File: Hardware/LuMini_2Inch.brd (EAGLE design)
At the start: 54.2 x 54.2 mm, 73 parts, among them J1 SOLDER_PAD_2, J2 SOLDER_PAD_2, J3 SOLDER_PAD_2

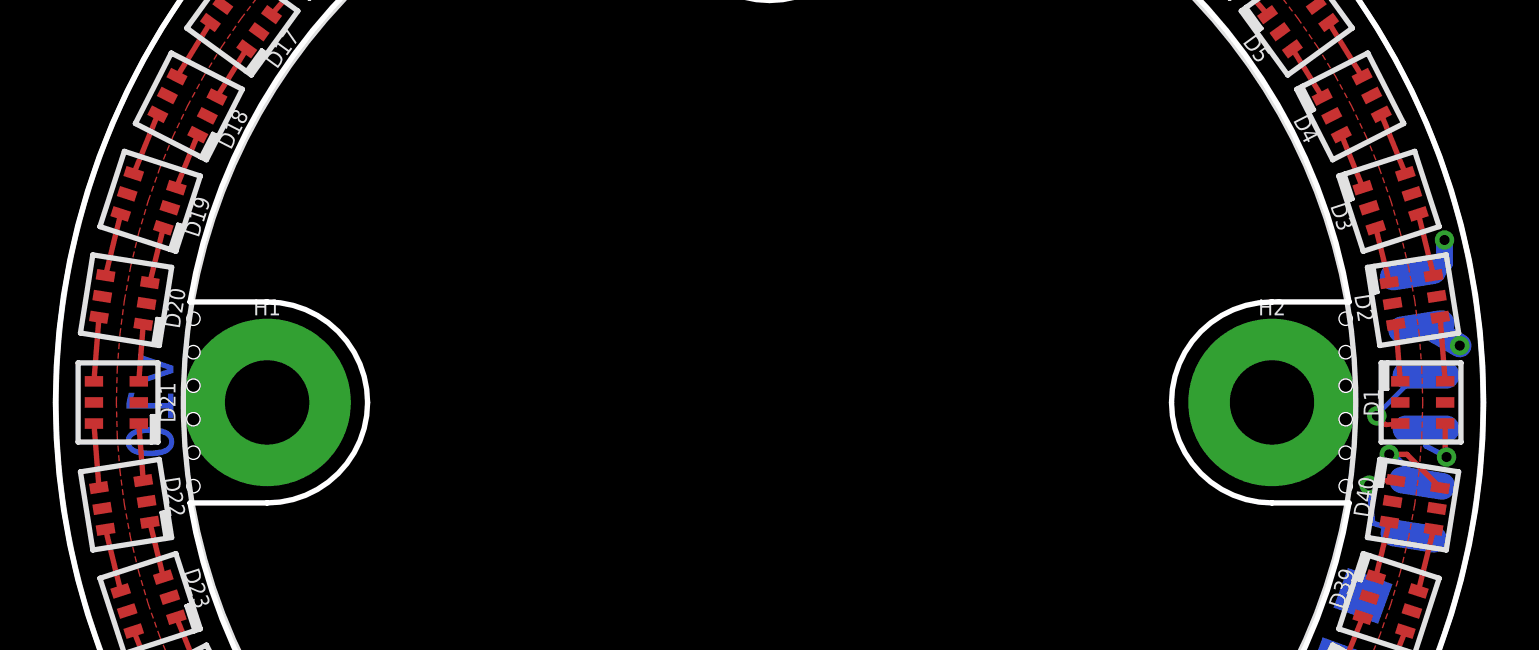
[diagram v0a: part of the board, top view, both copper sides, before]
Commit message: adding gnd via
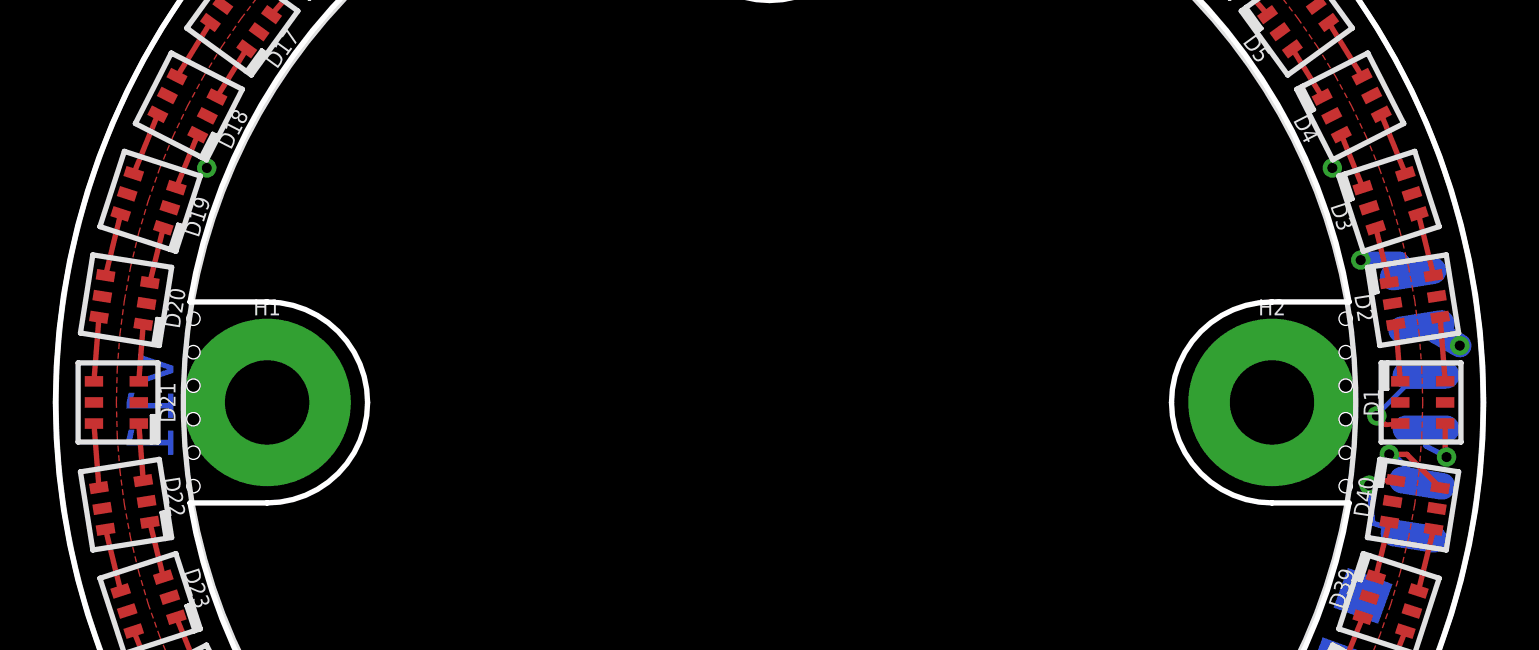
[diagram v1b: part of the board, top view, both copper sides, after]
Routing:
- net GND: vias 1 -> 3
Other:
- board text added: "v11"
- board text removed: "v10"
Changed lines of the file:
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@@
 <plain>
 <circle x="27.94" y="27.94" radius="27.051" width="0.2032" layer="21"/>
-<text x="5.334" y="29.845" size="1.778" layer="16" font="vector" ratio="15" rot="SMR270">v10</text>
+<text x="5.334" y="29.845" size="1.778" layer="16" font="vector" ratio="15" rot="SMR270">v11</text>
 <hole x="49.784" y="27.305" drill="0.508"/>
 <wire x1="5.969" y1="31.75" x2="8.89" y2="31.75" width="0.2032" layer="20"/>
@@
 <contactref element="D39" pad="GND"/>
 <contactref element="D40" pad="GND"/>
-<via x="53.5305" y="34.0995" extent="1-16" drill="0.381"/>
-<wire x1="53.5305" y1="34.0995" x2="53.5305" y2="33.2105" width="0.635" layer="16"/>
-<wire x1="53.136990625" y1="32.816990625" x2="52.342865625" y2="32.816990625" width="0.635" layer="16"/>
-<wire x1="53.5305" y1="33.2105" x2="53.136990625" y2="32.816990625" width="0.635" layer="16"/>
+<via x="50.3555" y="33.3375" extent="1-16" drill="0.381"/>
+<wire x1="51.82235625" y1="33.3375" x2="50.3555" y2="33.3375" width="0.635" layer="16"/>
 <contactref element="H1" pad="P1"/>
 <contactref element="H2" pad="P1"/>
@@
 <vertex x="6.4389" y="11.5189"/>
 </polygon>
+<via x="49.276" y="36.83" extent="1-16" drill="0.381"/>
+<via x="6.604" y="36.83" extent="1-16" drill="0.381"/>
+<wire x1="51.82235625" y1="33.3375" x2="52.342865625" y2="32.816990625" width="0.635" layer="16"/>
 <wire x1="50.44063125" y1="20.60686875" x2="50.6774" y2="20.5572625" width="0" layer="19" extent="1-16"/>
 </signal>

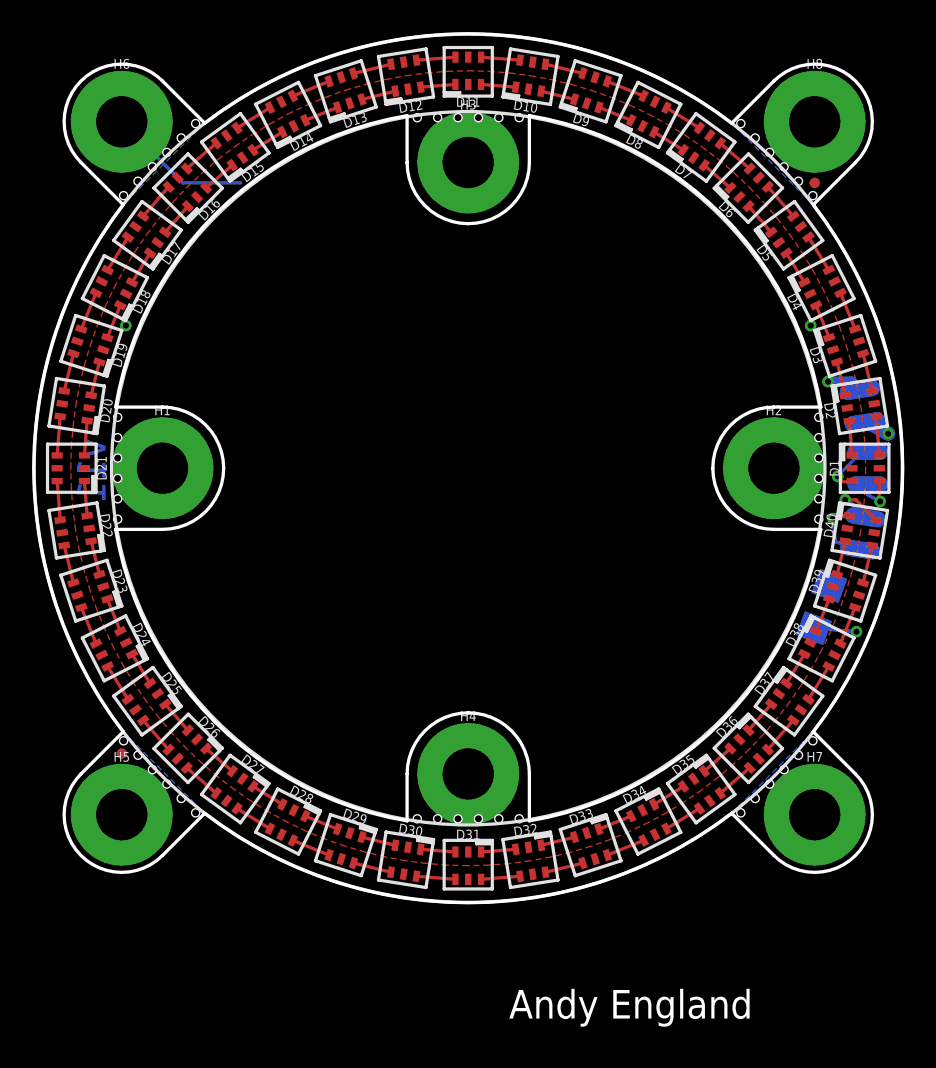
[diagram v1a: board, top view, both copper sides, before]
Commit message: updating gnd vias
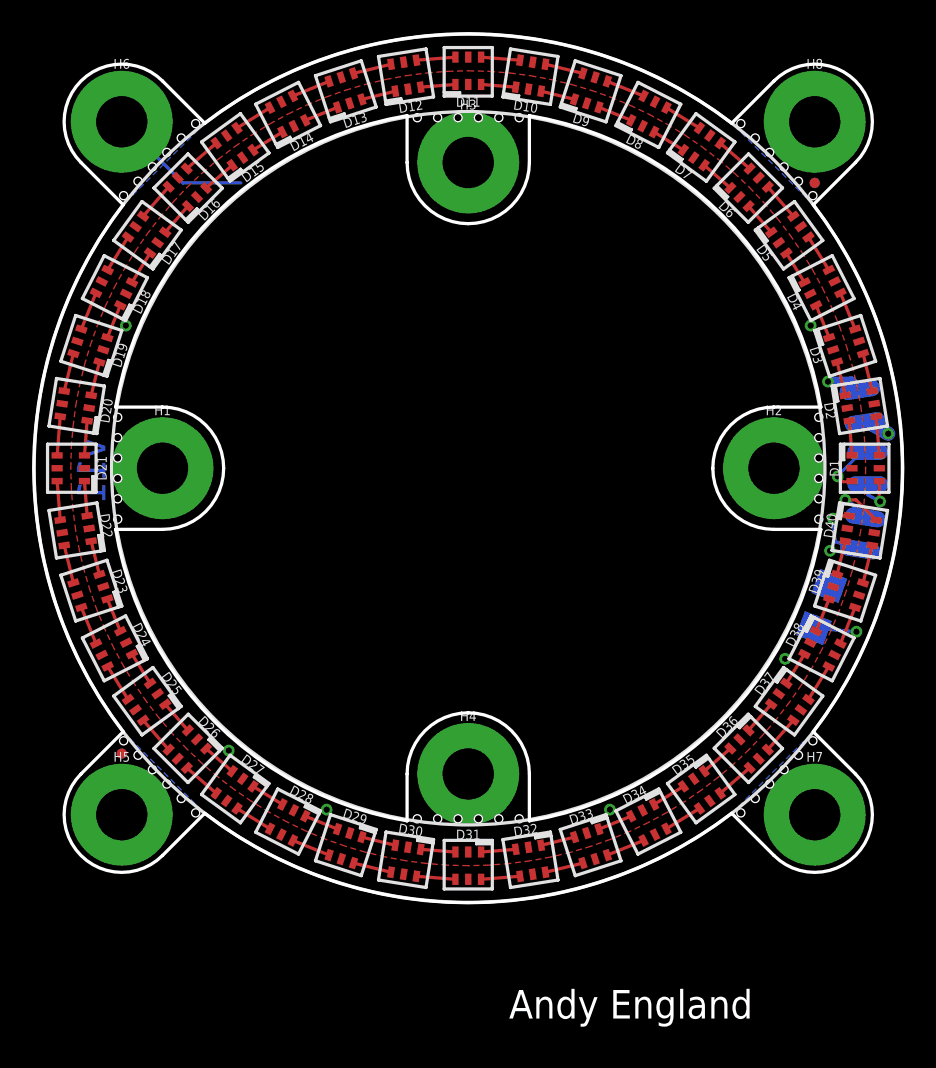
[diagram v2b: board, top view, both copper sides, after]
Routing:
- net GND: vias 3 -> 8
